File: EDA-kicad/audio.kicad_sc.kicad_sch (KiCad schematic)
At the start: 8 parts, among them J4 SJ2-35894B-SMT-TR, U3 CODEC-TLV320AIC3204IRHBR

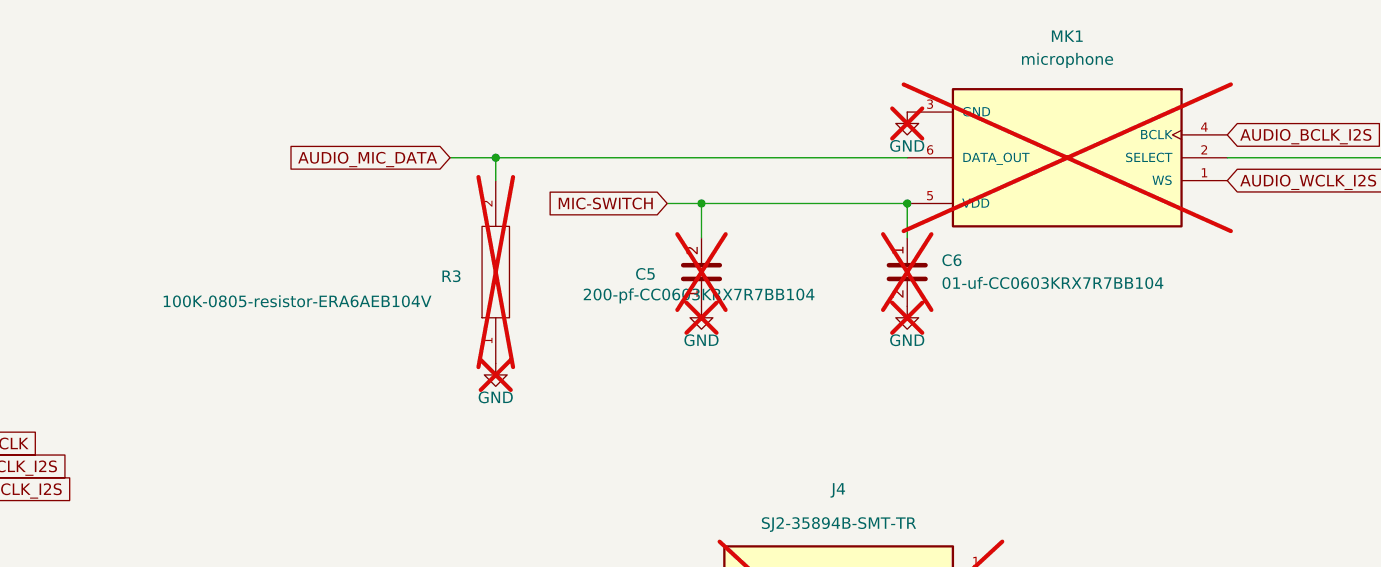
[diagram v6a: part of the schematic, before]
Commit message: Updated values of passive components
Updated values of passive components (resistors and capacitors) to include Ohm symbol, and removed microfarads symbol replaced by "uf" to fix BOM generator confusion.
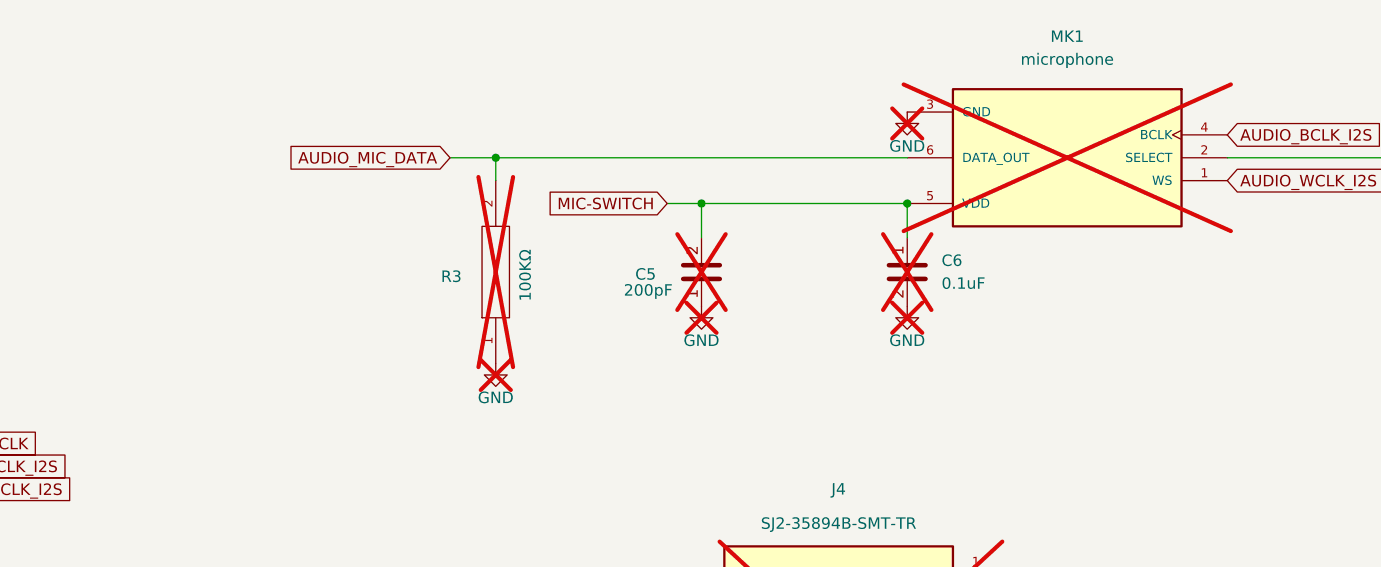
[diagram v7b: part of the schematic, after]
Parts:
- C5: value 200-pf-CC0603KRX7R7BB104 -> 200pF
- C6: value 01-uf-CC0603KRX7R7BB104 -> 0.1uF
- R3: value 100K-0805-resistor-ERA6AEB104V -> 100KΩ
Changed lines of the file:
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@@
 			)
 		)
-		(property "Value" "01-uf-CC0603KRX7R7BB104"
+		(property "Value" "0.1uF"
 			(at 199.39 74.93 90)
 			(effects
@@
 			)
 		)
-		(property "Value" "200-pf-CC0603KRX7R7BB104"
-			(at 159.512 76.2 90)
+		(property "Value" "200pF"
+			(at 164.084 75.692 90)
 			(effects
 				(font
@@
 			)
 		)
-		(property "Value" "100K-0805-resistor-ERA6AEB104V"
-			(at 112.776 76.962 90)
-			(effects
-				(font
+		(property "Value" "100KΩ"
+			(at 153.162 71.12 0)
+			(effects
+				(font
